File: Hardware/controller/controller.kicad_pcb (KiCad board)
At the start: 4 copper layers, 128.1 x 184.5 mm, 104 parts, among them J101 Conn_02x10_Odd_Even, J102 Conn_02x10_Odd_Even, J103 Conn_02x10_Odd_Even, J301 Conn_ARM_JTAG_SWD_10, J302 Conn_01x03_Male, Q301 MMBT3904, SW301 B3F-1005, SW302 B3F-1002, SW303 228ADS2AAWFCMBA, U101 PCA9543A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

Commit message: Added rear IO board
- Created the rear IO breakout board; it just provides Ethernet and USB
  out from the 20 pin expansion connector from the controller. It
  features a serial number EEPROM (to identify the available connections)
  and also an ADC to sense the USB VBus.

- Created footprints for the vertical USB and Ethernet connectors, and
  added them with 3D models
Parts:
- moved D301 18.0 mm to (66.5, 68.0)
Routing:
- net +3V3: track 102.3 -> 101.3 mm
- net Net-(D301-Pad2): track 14.9 -> 13.8 mm
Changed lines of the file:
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@@
   )
   (footprint "Diode_SMD:D_SMA_Handsoldering" (layer "F.Cu")
-    (at 66.5 86)
+    (at 66.5 68)
     (descr "Diode SMA (DO-214AC) Handsoldering")
     (tags "Diode SMA (DO-214AC) Handsoldering")
@@
     (property "Sheetname" "CPU")
     (attr through_hole)
-    (fp_text reference "LS301" (at 0 -7 unlocked) (layer "F.SilkS")
+    (fp_text reference "LS301" (at 0 7.5 unlocked) (layer "F.SilkS")
       (effects (font (size 1 1) (thickness 0.15)))
     )
@@
   (segment (start 88.5625 51.25) (end 87.35 51.25) (width 0.4064) (layer "F.Cu") (net 60))
   (segment (start 88.8875 65.5125) (end 88.9 65.5) (width 0.254) (layer "F.Cu") (net 60))
-  (segment (start 63.25 85.25) (end 64 86) (width 0.635) (layer "F.Cu") (net 60))
   (segment (start 141.2 58.0125) (end 141.2 56.6) (width 1.27) (layer "F.Cu") (net 60))
   (segment (start 85.6625 51.25) (end 87.4 51.25) (width 0.3) (layer "F.Cu") (net 60))
@@
   (segment (start 54.8 28.9) (end 53.7 28.9) (width 0.2032) (layer "F.Cu") (net 60))
   (segment (start 45.5 32.75) (end 45.5 31.4) (width 0.635) (layer "F.Cu") (net 60))
-  (segment (start 63.25 76.5) (end 63.25 85.25) (width 0.635) (layer "F.Cu") (net 60))
+  (segment (start 63.25 67.725) (end 63.25 76.475) (width 0.635) (layer "F.Cu") (net 60))
   (segment (start 77.7 39.085403) (end 77.7 38.4375) (width 0.254) (layer "F.Cu") (net 60))
   (segment (start 87 44.25) (end 88.1375 44.25) (width 0.635) (layer "F.Cu") (net 60))
@@
   (segment (start 28.5 38.9) (end 28.5 38.4) (width 0.2032) (layer "B.Cu") (net 109))
   (segment (start 28.5 26.5) (end 28.5 32.1) (width 0.4064) (layer "F.Cu") (net 110))
-  (segment (start 69.75 85.25) (end 69 86) (width 0.635) (layer "F.Cu") (net 111))
-  (segment (start 69.75 76.5) (end 69.75 85.25) (width 0.635) (layer "F.Cu") (net 111))
+  (segment (start 69.75 67.725) (end 69.75 76.475) (width 0.635) (layer "F.Cu") (net 111))
   (segment (start 74.7625 76.6) (end 69.85 76.6) (width 0.6) (layer "F.Cu") (net 111))
   (segment (start 69.85 76.6) (end 69.75 76.5) (width 0.635) (layer "F.Cu") (net 111))

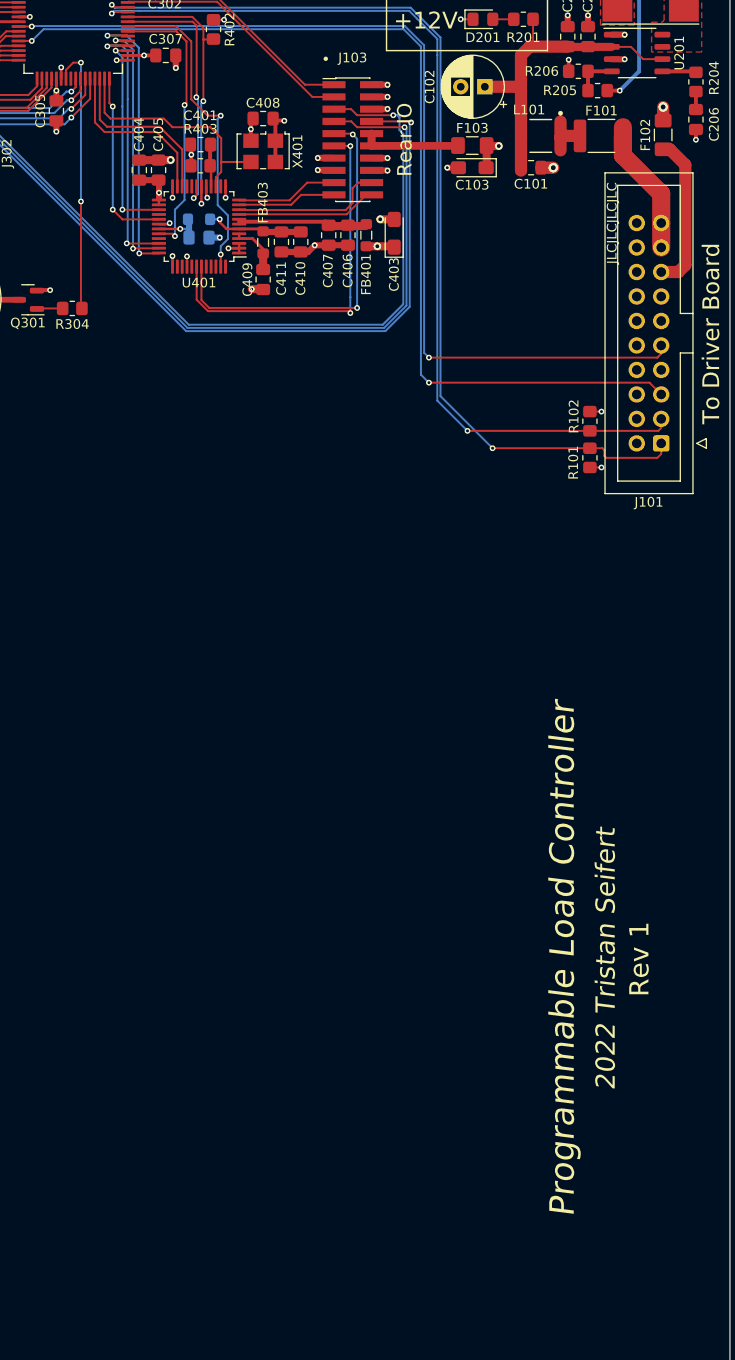
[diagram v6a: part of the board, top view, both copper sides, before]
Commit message: External trigger input
- Added a basic Schmitt-trigger based external trigger input. There's a
  basic pulse shaping circuit attached to it, before its fed into the
  buffer, and then off to the main board to use as an interrupt line to
  control the system mode.
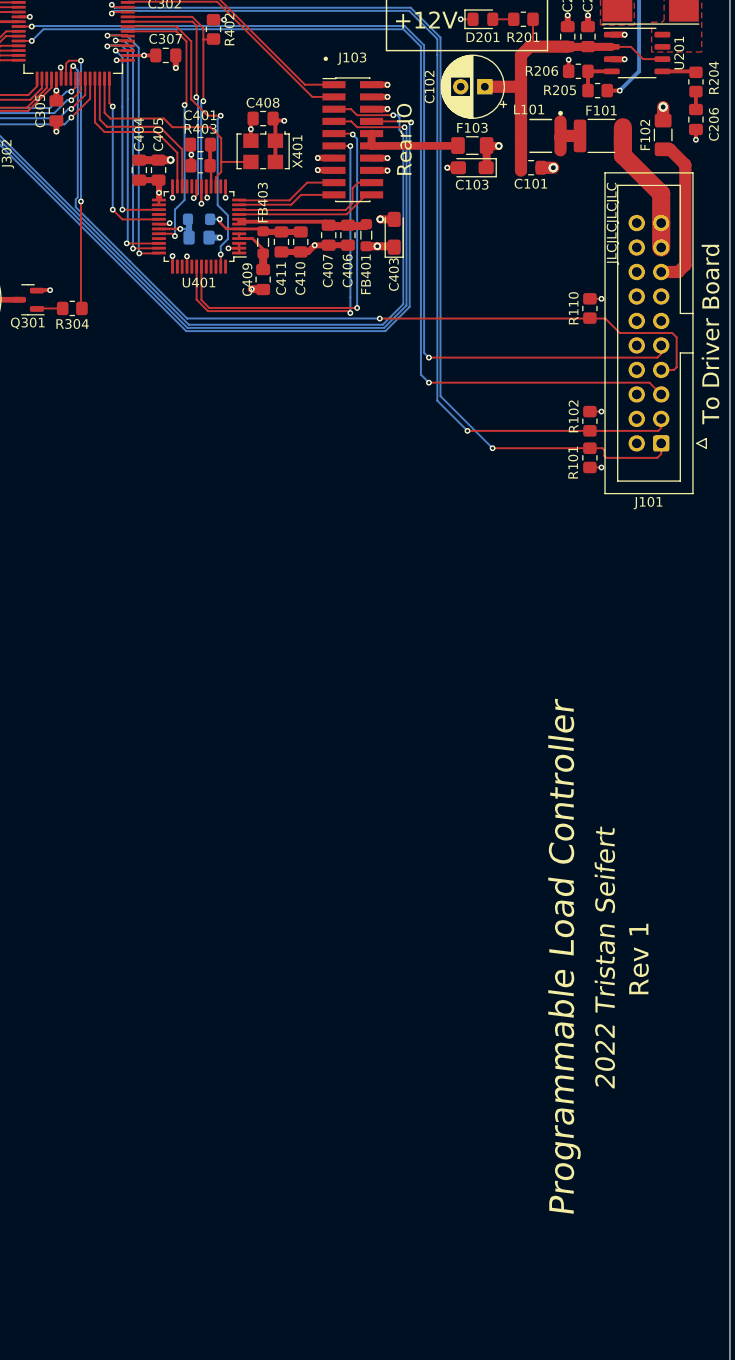
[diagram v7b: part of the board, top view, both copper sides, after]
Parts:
- added R110: 10k, Resistor_SMD:R_0805_2012Metric_Pad1.20x1.40mm_HandSolder, F.Cu at (133.6, 77.5)
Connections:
- J101 pad 7: /~{EXT_ACTIVE} -> /~{EXT_TRIG}
- U302 pad 24: unconnected-(U302-Pad24) -> /~{EXT_TRIG}
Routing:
- net /~{EXT_TRIG}: track 0.00 -> 89.1 mm, vias 0 -> 2
- net +3V3: track 101.3 -> 102.5 mm, vias 39 -> 40
- net /CPU/BEEPER: track 28.8 -> 29.4 mm

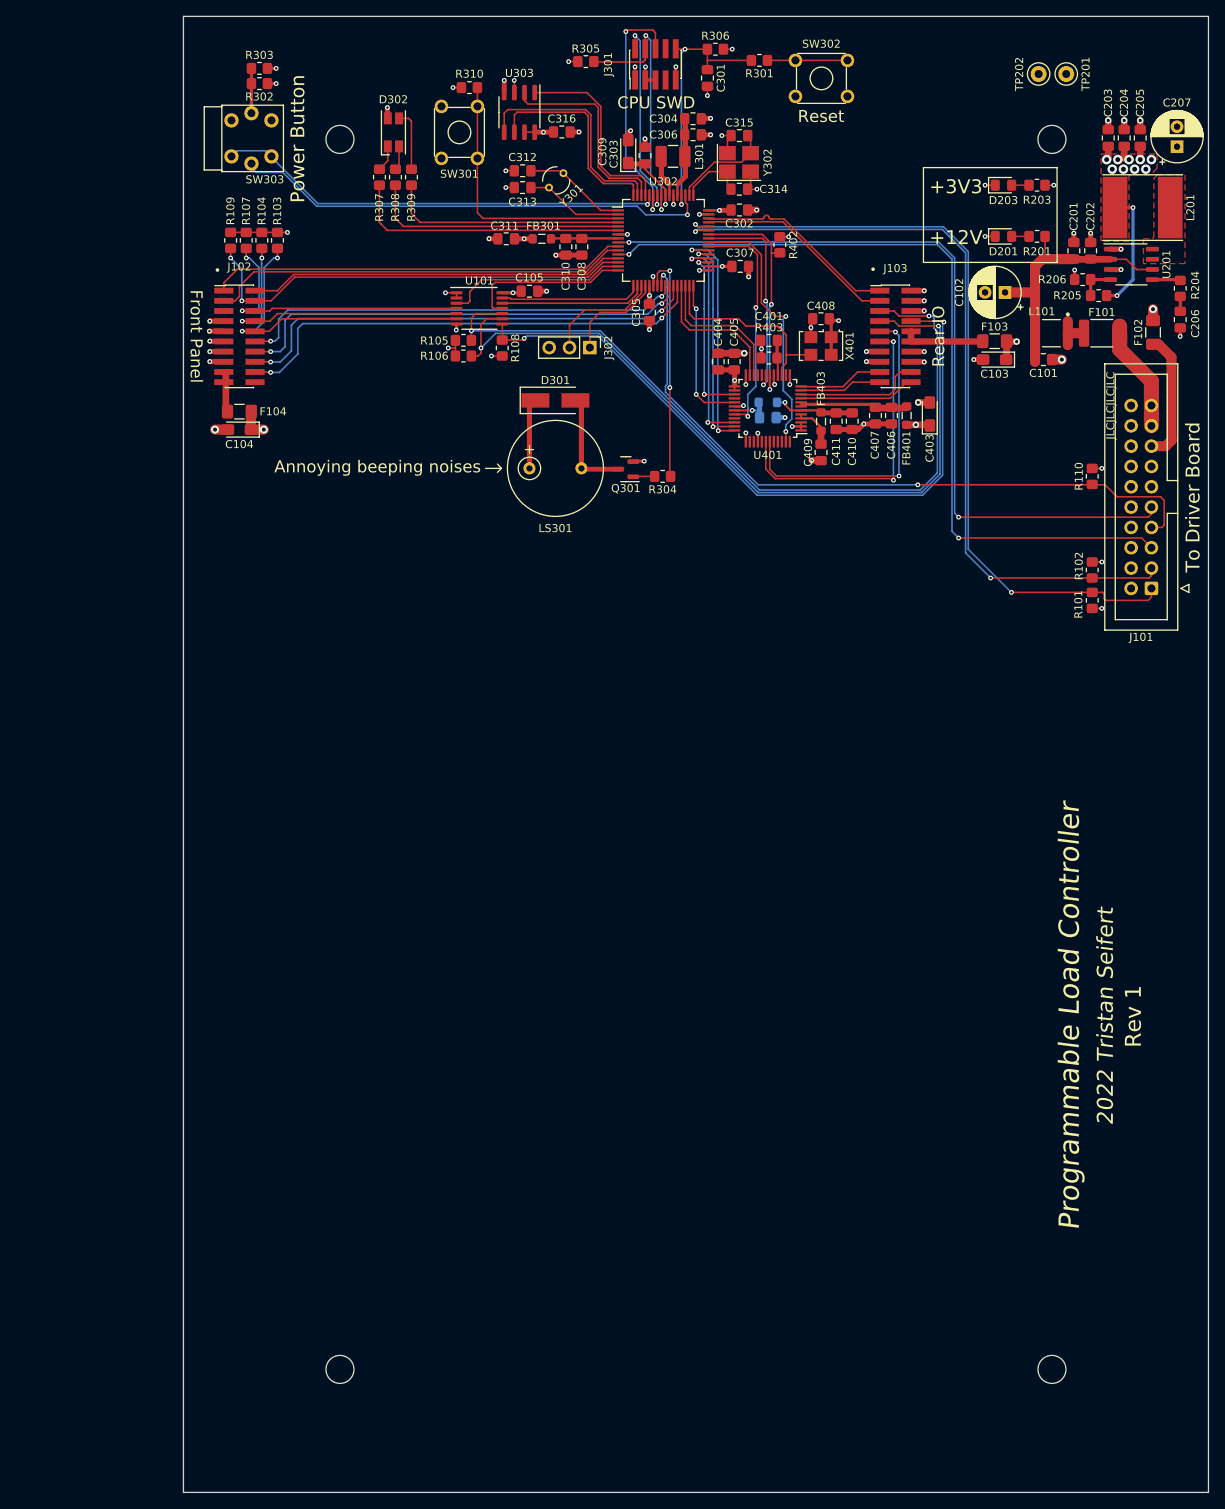
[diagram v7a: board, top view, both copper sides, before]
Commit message: Controller board fan controller
- Added a fan controller (the same EMC2101-R as on the driver) to the
  controller board, to control the rear case fan. This is driven off the
  rear IO I2C bus, which itself is switched behind the "auxiliary" I2C
  bus.
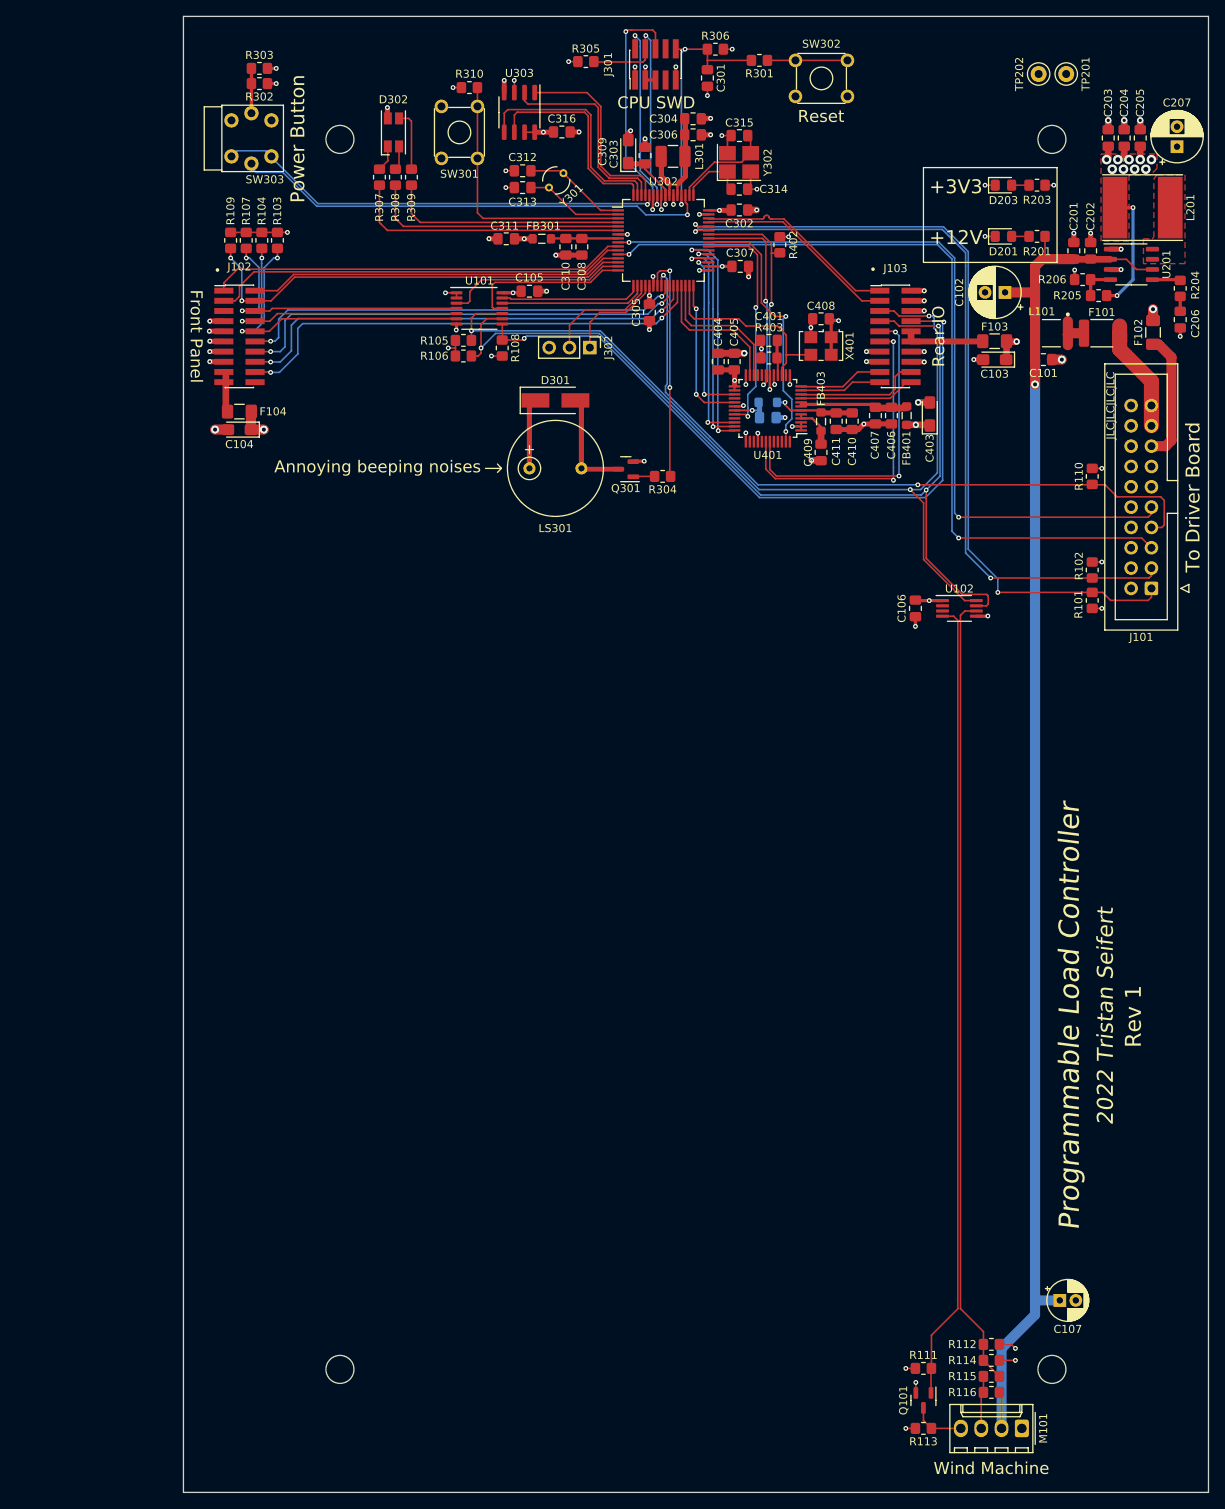
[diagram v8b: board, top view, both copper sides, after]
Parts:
- added C106: 100nF, Capacitor_SMD:C_0805_2012Metric_Pad1.18x1.45mm_HandSolder, F.Cu at (111.5, 94.0)
- added C107: 10µF, Capacitor_THT:CP_Radial_D5.0mm_P2.00mm, F.Cu at (129.5, 180.5)
- added M101: Fan_4pin, Connector_Molex:Molex_KK-254_AE-6410-04A_1x04_P2.54mm_Vertical, F.Cu at (124.8, 196.5)
- added Q101: MMBT3904, Package_TO_SOT_SMD:SOT-23, F.Cu at (112.5, 193.0)
- added R111: 10k, Resistor_SMD:R_0805_2012Metric_Pad1.20x1.40mm_HandSolder, F.Cu at (112.5, 189.0)
- added R112: 10k, Resistor_SMD:R_0805_2012Metric_Pad1.20x1.40mm_HandSolder, F.Cu at (121.0, 186.0)
- added R113: 4k7, Resistor_SMD:R_0805_2012Metric_Pad1.20x1.40mm_HandSolder, F.Cu at (112.5, 196.5)
- added R114: 10k, Resistor_SMD:R_0805_2012Metric_Pad1.20x1.40mm_HandSolder, F.Cu at (121.0, 188.0)
- added R115: 27k4, Resistor_SMD:R_0805_2012Metric_Pad1.20x1.40mm_HandSolder, F.Cu at (121.0, 190.0)
- added R116: 4k7, Resistor_SMD:R_0805_2012Metric_Pad1.20x1.40mm_HandSolder, F.Cu at (121.0, 192.0)
- added U102: EMC2101-R, Package_SO:MSOP-8_3x3mm_P0.65mm, F.Cu at (117.0, 94.0)
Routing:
- net +12V: track 33.6 -> 176.6 mm, vias 0 -> 1
- net /FAN_PWM: track 0.00 -> 100.1 mm
- net /FAN_TACH: track 0.00 -> 99.4 mm
- net /IO_SDA: track 101.4 -> 122.6 mm, vias 2 -> 3
- net /IO_SCL: track 100.9 -> 119.1 mm, vias 2 -> 3
- net +3V3: track 102.5 -> 110.5 mm, vias 40 -> 44
- net Net-(M101-Pad3): track 0.00 -> 6.62 mm
- net Net-(M101-Pad4): track 0.00 -> 6.16 mm
- net GND: track 106.9 -> 112.9 mm, vias 67 -> 71
- net /EXT_SCL: track 101.6 -> 102.3 mm
- net /~{IO_IRQ}: track 89.9 -> 90.5 mm
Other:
- board text added: "Wind Machine"
